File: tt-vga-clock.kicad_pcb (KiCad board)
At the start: 4 copper layers, 41 x 55.9 mm, 69 parts, among them J1 USB_C_Receptacle_USB2.0, J3 Conn_02x04_Odd_Even, J5 DE15_Receptacle_HighDensity_M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, SW2 B3U-1000P, SW3 B3U-1000P, SW4 B3U-1000P, SW5 B3U-1000P, U1 Caravel_QFN, U2 W25Q32JVSS, U3 AZ1117-3.3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

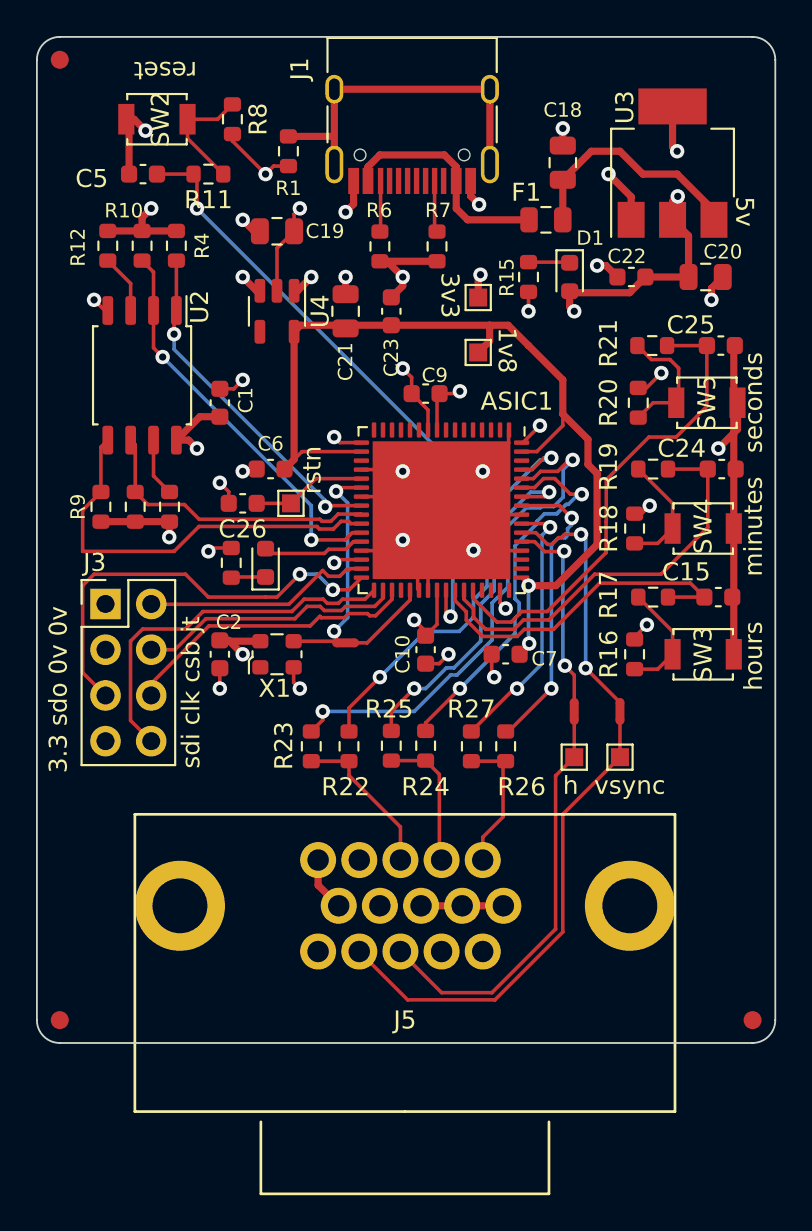
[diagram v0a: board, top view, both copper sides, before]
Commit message: Increase space (ASIC east) for next rev; tidy west/south traces
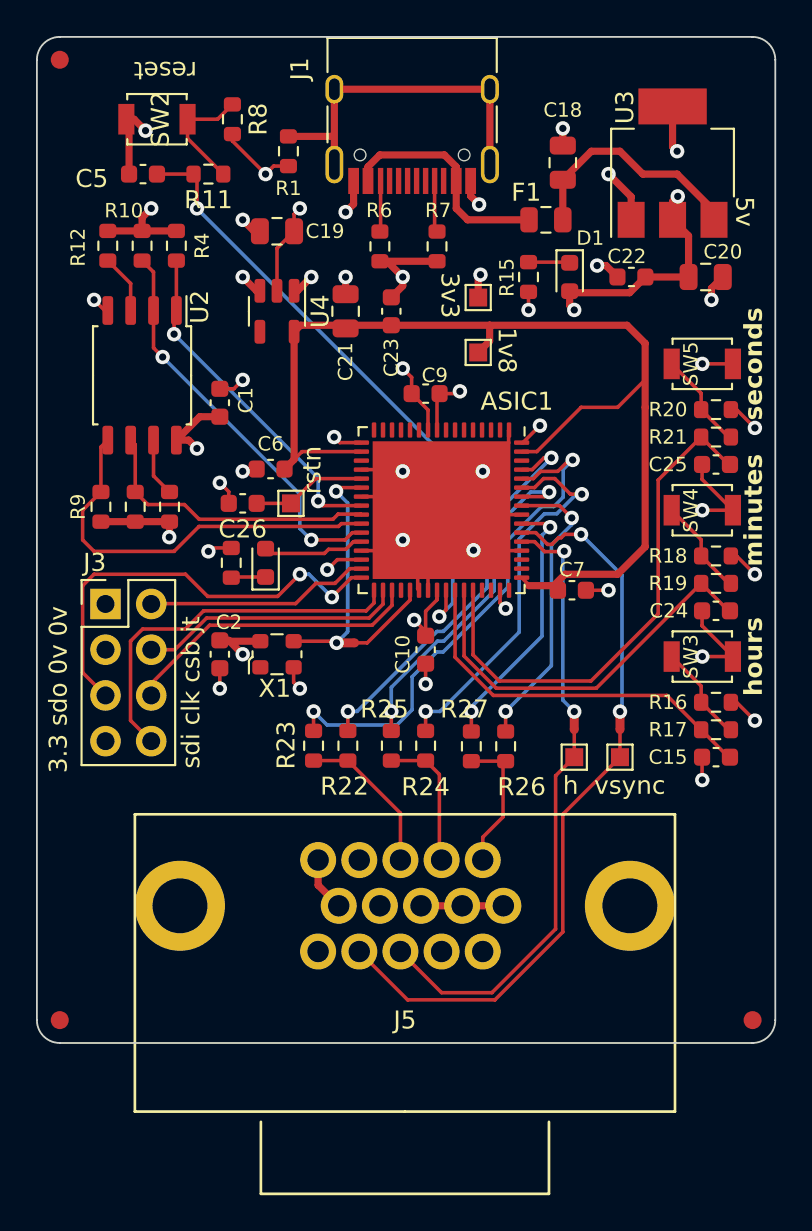
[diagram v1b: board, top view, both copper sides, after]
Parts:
- moved C15 8.89 mm to (125.4, 63.1), turned to 0 degrees
- moved R17 8.15 mm to (125.4, 61.6), turned to 180 degrees
- moved C24 7.88 mm to (125.4, 55.0), turned to 0 degrees
- moved R19 7.25 mm to (125.4, 53.5), turned to 180 degrees
- moved C25 6.61 mm to (125.4, 46.9), turned to 0 degrees
- moved R21 6.19 mm to (125.4, 45.3), turned to 180 degrees
- moved R16 5.25 mm to (125.4, 60.1), turned to 0 degrees
- moved C7 5.12 mm to (117.4, 53.9), turned to 180 degrees
- moved R18 4.77 mm to (125.4, 51.9), turned to 0 degrees
- moved R20 4.33 mm to (125.4, 43.8), turned to 0 degrees
- moved SW5 2.17 mm to (124.7, 41.3)
- moved SW4 1.02 mm to (124.7, 49.4)
- moved NT1 0.51 mm to (117.6, 61.1)
- moved NT2 0.51 mm to (120.1, 61.1)
- moved SW3 0.14 mm to (124.7, 57.5)
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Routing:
- net +1V8: track 53.5 -> 62.1 mm, vias 2 -> 0
- net +3V3: track 76.5 -> 69.7 mm, vias 19 -> 22
- net /prj_io8: track 19.1 -> 21.3 mm
- net /prj_io10: track 26.9 -> 29.1 mm
- net Net-(R20-Pad1): track 7.24 -> 5.50 mm
- net Net-(R18-Pad1): track 6.54 -> 5.50 mm
- net GND: track 96.4 -> 97.4 mm
- net Net-(R16-Pad1): track 6.42 -> 5.50 mm
- net /prj_io23: track 23.2 -> 22.4 mm
- net /prj_io17: track 14.0 -> 14.6 mm
- net flash_io0: track 23.1 -> 22.5 mm
- net /prj_io9: track 22.8 -> 22.2 mm
- net /vsync: track 27.0 -> 26.5 mm
- net /hsync: track 23.0 -> 22.5 mm
- net /prj_io16: track 11.3 -> 11.8 mm
